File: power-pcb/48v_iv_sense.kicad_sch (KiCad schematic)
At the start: 20 parts, among them J21 Screw_Terminal_01x03, U2 ISO1540, U5 ADS1015IDGS, U7 INA240A1D

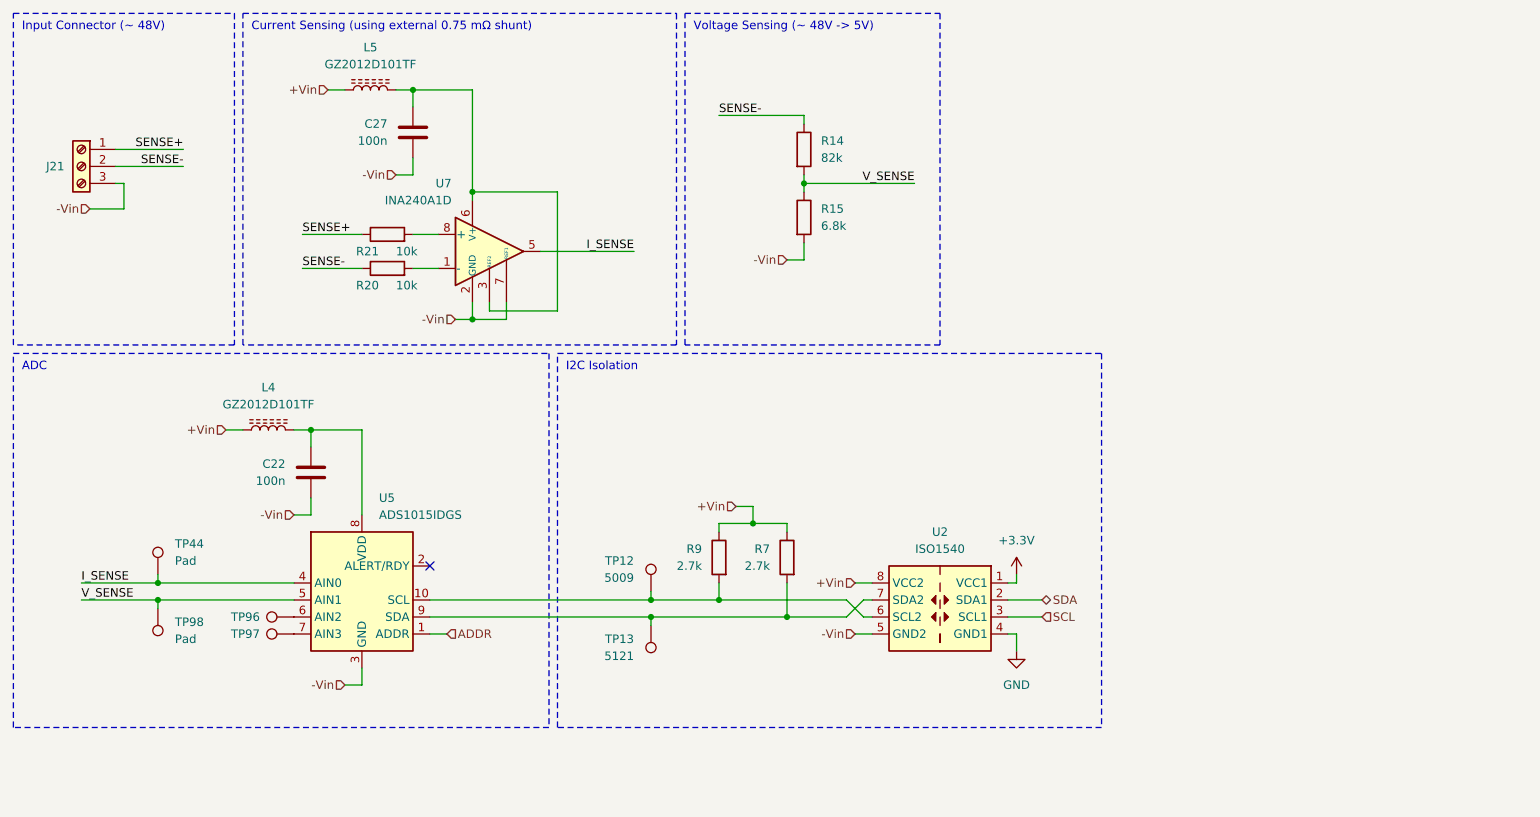
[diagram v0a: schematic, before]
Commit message: power-pcb: finish schematic layout
All parts are placed and connected, ERC passes (except for two
exclusions with comment).
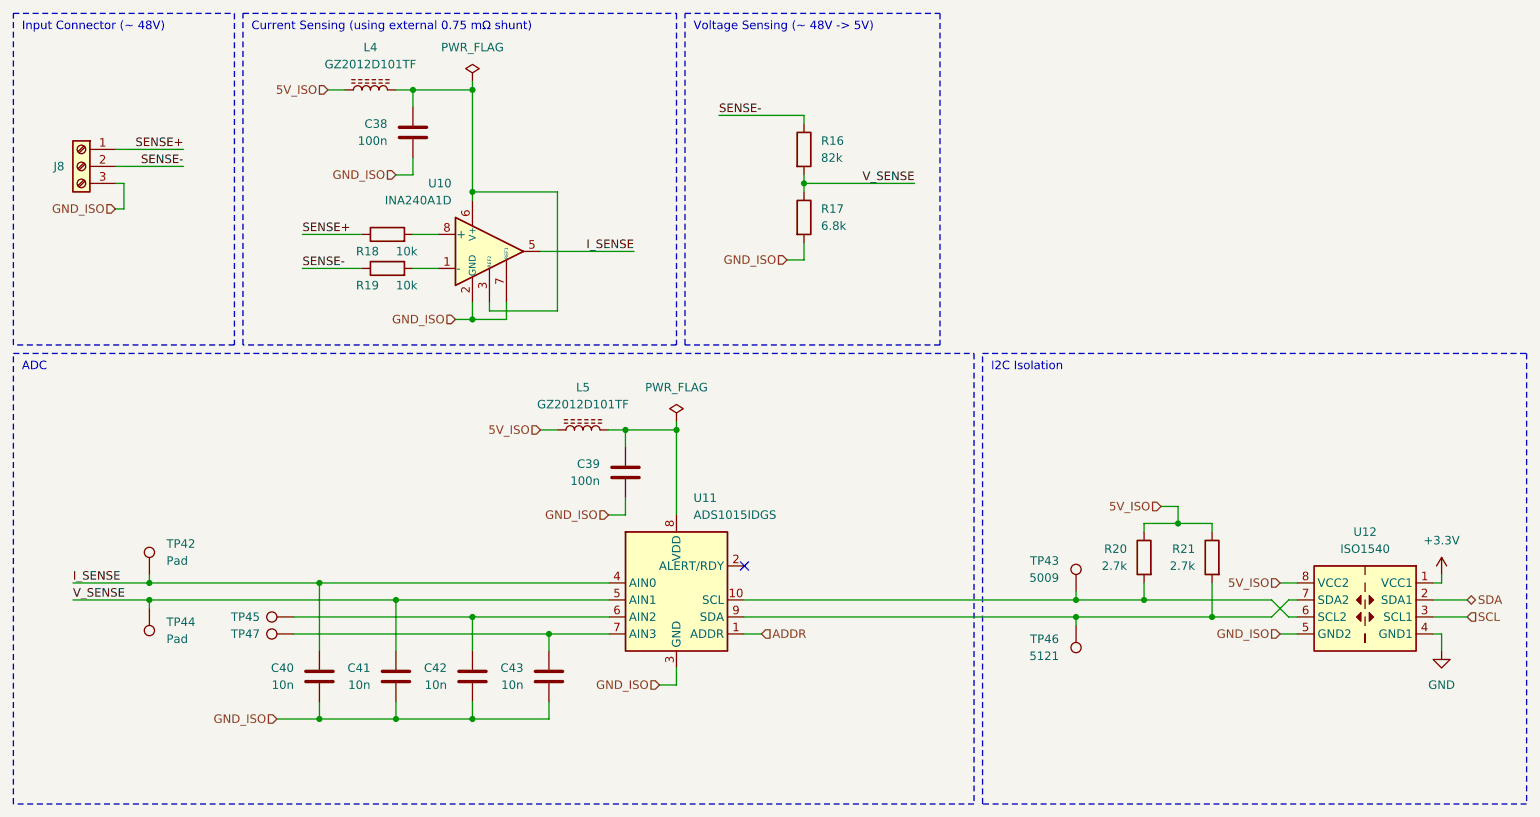
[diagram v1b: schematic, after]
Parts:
- added C40, C41, C42, C43: 10n, symbol Device:C
- renumbered C27 to C38, C22 to C39, J21 to J8, L5 to L4, L4 to L5, R14 to R16, R15 to R17, R21 to R18, R20 to R19, R9 to R20, R7 to R21, TP44 to TP42, TP12 to TP43, TP98 to TP44, TP96 to TP45, TP13 to TP46, TP97 to TP47, U7 to U10, U5 to U11, U2 to U12
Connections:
- net I_SENSE: now also C40.1
- net V_SENSE: now also C41.1
- net at TP45.1, U11.6 (AIN2): now also C42.1
- net at TP47.1, U11.7 (AIN3): now also C43.1
- net +Vin renamed 5V_ISO
- net -Vin renamed GND_ISO
- net GND_ISO: now also C40.2, C41.2, C42.2, C43.2
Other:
- moved on the sheet: C39, L5, R20, R21, TP42, TP43, TP44, TP46, U11, U12

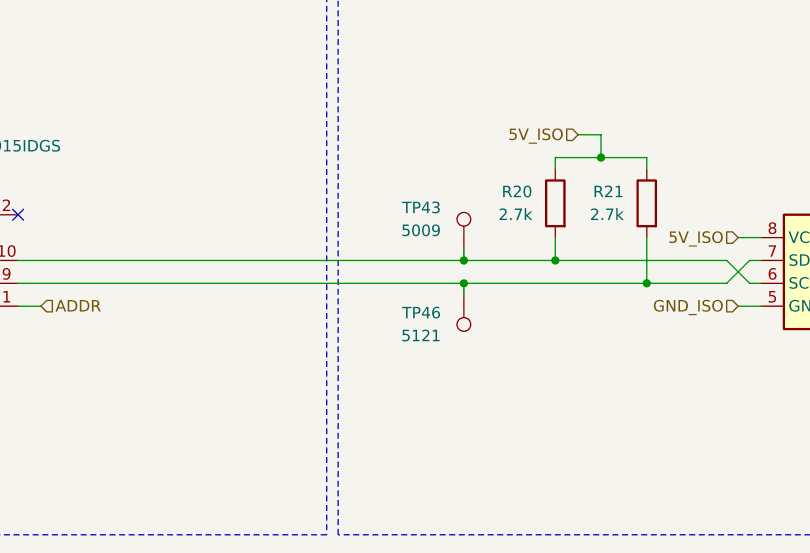
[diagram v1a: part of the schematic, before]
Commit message: power-pcb: finish assigning JLCPCB PN
Also assigned missing footprints.
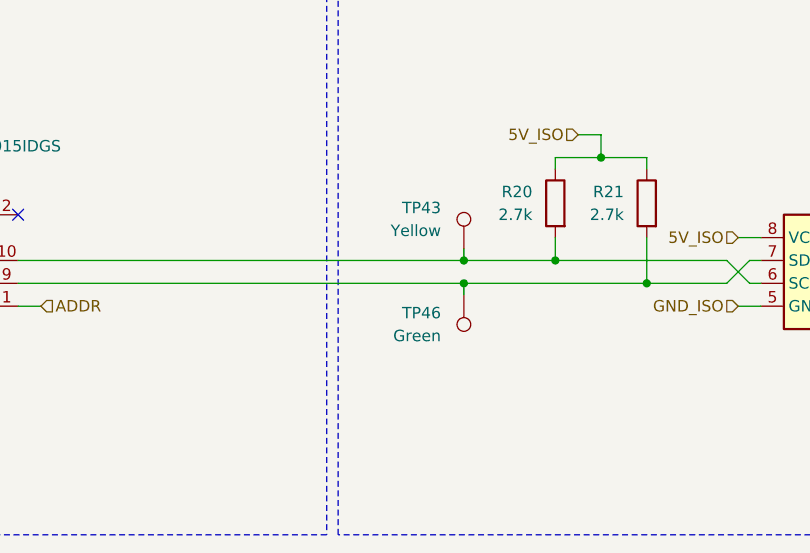
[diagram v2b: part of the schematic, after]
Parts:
- C40, C41, C42, C43: footprint (none) -> Capacitor_SMD:C_0402_1005Metric_Pad0.74x0.62mm_HandSolder; JLCPCB (none) -> C15195
- J8: footprint (none) -> Exocet:Wuerth_Term_Blk_3pos_Side_Entry_5mm; MFR (none) -> Wuerth Eletronik; MPN (none) -> 691137710003
- R16: footprint Capacitor_SMD:C_0603_1608Metric_Pad1.08x0.95mm_HandSolder -> Resistor_SMD:R_0603_1608Metric_Pad0.98x0.95mm_HandSolder
- R17: footprint Capacitor_SMD:C_0603_1608Metric_Pad1.08x0.95mm_HandSolder -> Resistor_SMD:R_0603_1608Metric_Pad0.98x0.95mm_HandSolder; JLCPCB C23254 -> C23212
- R18, R19: footprint (none) -> Resistor_SMD:R_0603_1608Metric_Pad0.98x0.95mm_HandSolder; JLCPCB (none) -> C25804
- R20, R21: footprint (none) -> Resistor_SMD:R_0603_1608Metric_Pad0.98x0.95mm_HandSolder; JLCPCB (none) -> C13167
- TP42, TP44: footprint (none) -> TestPoint:TestPoint_Pad_D1.5mm
- TP43: value 5009 -> Yellow; footprint (none) -> TestPoint:TestPoint_Keystone_5005-5009_Compact; MFR (none) -> Keystone Electronics; MPN (none) -> 5009
- TP45, TP47: value TestPoint -> Hole
- TP46: value 5121 -> Green; footprint (none) -> TestPoint:TestPoint_Keystone_5005-5009_Compact; MFR (none) -> Keystone Electronics; MPN (none) -> 5121
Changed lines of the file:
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@@
 			)
 		)
-		(property "Footprint" "Capacitor_SMD:C_0603_1608Metric_Pad1.08x0.95mm_HandSolder"
+		(property "Footprint" "Resistor_SMD:R_0603_1608Metric_Pad0.98x0.95mm_HandSolder"
 			(at 129.032 43.18 90)
 			(hide yes)
@@
 			)
 		)
-		(property "JLCPCB" "C23254"
+		(property "JLCPCB" "C23212"
 			(at 130.81 43.18 0)
 			(hide yes)
@@
 			)
 		)
-		(property "Footprint" ""
+		(property "Footprint" "Exocet:Wuerth_Term_Blk_3pos_Side_Entry_5mm"
 			(at 22.86 35.56 0)
 			(hide yes)
@@
 		)
 		(property "Description" "Generic screw terminal, single row, 01x03, script generated (kicad-library-utils/schlib/autogen/connector/)"
+			(at 22.86 35.56 0)
+			(hide yes)
+			(show_name no)
+			(do_not_autoplace no)
+			(effects
+				(font
+					(size 1.27 1.27)
+				)
+			)
+		)
+		(property "MFR" "Wuerth Eletronik"
+			(at 22.86 35.56 0)
+			(hide yes)
+			(show_name no)
+			(do_not_autoplace no)
+			(effects
+				(font
+					(size 1.27 1.27)
+				)
+			)
+		)
+		(property "MPN" "691137710003"
 			(at 22.86 35.56 0)
 			(hide yes)
@@
 			)
 		)
-		(property "Footprint" ""
+		(property "Footprint" "Capacitor_SMD:C_0402_1005Metric_Pad0.74x0.62mm_HandSolder"
 			(at 80.3148 115.57 0)
 			(hide yes)
@@
 			)
 		)
-		(property "Description" "Unpolarized capacitor"
+		(property "Description" "50V X7R ±10%"
+			(at 81.28 111.76 0)
+			(hide yes)
+			(show_name no)
+			(do_not_autoplace no)
+			(effects
+				(font
+					(size 1.27 1.27)
+				)
+			)
+		)
+		(property "JLCPCB" "C15195"
 			(at 81.28 111.76 0)
 			(hide yes)
@@
 			)
 		)
-		(property "Footprint" ""
+		(property "Footprint" "Capacitor_SMD:C_0402_1005Metric_Pad0.74x0.62mm_HandSolder"
 			(at 68.8848 115.57 0)
 			(hide yes)
@@
 			)
 		)
-		(property "Description" "Unpolarized capacitor"
+		(property "Description" "50V X7R ±10%"
+			(at 69.85 111.76 0)
+			(hide yes)
+			(show_name no)
+			(do_not_autoplace no)
+			(effects
+				(font
+					(size 1.27 1.27)
+				)
+			)
+		)
+		(property "JLCPCB" "C15195"
 			(at 69.85 111.76 0)
 			(hide yes)
@@
 			)
 		)
-		(property "Value" "5009"
+		(property "Value" "Yellow"
 			(at 168.91 97.0279 0)
 			(show_name no)
@@
 			)
 		)
-		(property "Footprint" ""
+		(property "Footprint" "TestPoint:TestPoint_Keystone_5005-5009_Compact"
 			(at 166.37 99.06 0)
 			(hide yes)
@@
 			)
 		)
-		(property "Description" "Auxiliary Battery GND"
+		(property "Description" "Test Point"
+			(at 171.45 99.06 0)
+			(hide yes)
+			(show_name no)
+			(do_not_autoplace no)
+			(effects
+				(font
+					(size 1.27 1.27)
+				)
+			)
+		)
+		(property "MPN" "5009"
+			(at 171.45 99.06 0)
+			(hide yes)
+			(show_name no)
+			(do_not_autoplace no)
+			(effects
+				(font
+					(size 1.27 1.27)
+				)
+			)
+		)
+		(property "MFR" "Keystone Electronics"
 			(at 171.45 99.06 0)
 			(hide yes)
@@
 			)
 		)
-		(property "Footprint" ""
+		(property "Footprint" "Resistor_SMD:R_0603_1608Metric_Pad0.98x0.95mm_HandSolder"
 			(at 193.548 93.98 90)
 			(hide yes)
@@
 		)
 		(property "Description" "Resistor"
+			(at 191.77 93.98 0)
+			(hide yes)
+			(show_name no)
+			(do_not_autoplace no)
+			(effects
+				(font
+					(size 1.27 1.27)
+				)
+			)
+		)
+		(property "JLCPCB" "C13167"
 			(at 191.77 93.98 0)
 			(hide yes)
@@
 			)
 		)
-		(property "Footprint" ""
+		(property "Footprint" "Resistor_SMD:R_0603_1608Metric_Pad0.98x0.95mm_HandSolder"
 			(at 68.58 52.578 90)
 			(hide yes)
@@
 		(property "Description" "Resistor"
 			(at 68.58 50.8 0)
+			(hide yes)
+			(show_name no)
+			(do_not_autoplace no)
+			(effects
+				(font
+					(size 1.27 1.27)
+				)
+			)
+		)
+		(property "JLCPCB" "C25804"
+			(at 68.58 50.8 90)
 			(hide yes)
 			(show_name no)
@@
 			)
 		)
-		(property "Footprint" ""
+		(property "Footprint" "TestPoint:TestPoint_Pad_D1.5mm"
 			(at 38.1 96.52 0)
 			(hide yes)
@@
 			)
 		)
-		(property "Description" "test point"
+		(property "Description" "Test Point"
 			(at 33.02 96.52 0)
 			(hide yes)
@@
 			)
 		)
-		(property "Value" "5121"
+		(property "Value" "Green"
 			(at 168.91 108.7119 0)
 			(show_name no)
@@
 			)
 		)
-		(property "Footprint" ""
+		(property "Footprint" "TestPoint:TestPoint_Keystone_5005-5009_Compact"
 			(at 176.53 104.14 0)
 			(hide yes)
@@
 			)
 		)
-		(property "Description" "Auxiliary Battery GND"
+		(property "Description" "Test Point"
+			(at 171.45 104.14 0)
+			(hide yes)
+			(show_name no)
+			(do_not_autoplace no)
+			(effects
+				(font
+					(size 1.27 1.27)
+				)
+			)
+		)
+		(property "MPN" "5121"
+			(at 171.45 104.14 0)
+			(hide yes)
+			(show_name no)
+			(do_not_autoplace no)
+			(effects
+				(font
+					(size 1.27 1.27)
+				)
+			)
+		)
+		(property "MFR" "Keystone Electronics"
 			(at 171.45 104.14 0)
 			(hide yes)
@@
 			)
 		)
-		(property "Value" "TestPoint"
+		(property "Value" "Hole"
 			(at 49.53 104.1399 90)
 			(hide yes)
@@
 			)
 		)
-		(property "Description" "test point"
+		(property "Description" "Test Point"
 			(at 54.61 102.87 0)
 			(hide yes)
@@
 			)
 		)
-		(property "Footprint" ""
+		(property "Footprint" "TestPoint:TestPoint_Pad_D1.5mm"
 			(at 27.94 101.6 0)
 			(hide yes)
@@
 			)
 		)
-		(property "Description" "test point"
+		(property "Description" "Test Point"
 			(at 33.02 101.6 0)
 			(hide yes)
@@
 			)
 		)
-		(property "Footprint" "Capacitor_SMD:C_0603_1608Metric_Pad1.08x0.95mm_HandSolder"
+		(property "Footprint" "Resistor_SMD:R_0603_1608Metric_Pad0.98x0.95mm_HandSolder"
 			(at 129.032 33.02 90)
 			(hide yes)
@@
 			)
 		)
-		(property "Footprint" ""
+		(property "Footprint" "Resistor_SMD:R_0603_1608Metric_Pad0.98x0.95mm_HandSolder"
 			(at 68.58 47.498 90)
 			(hide yes)
@@
 		(property "Description" "Resistor"
 			(at 68.58 45.72 0)
+			(hide yes)
+			(show_name no)
+			(do_not_autoplace no)
+			(effects
+				(font
+					(size 1.27 1.27)
+				)
+			)
+		)
+		(property "JLCPCB" "C25804"
+			(at 68.58 45.72 90)
 			(hide yes)
 			(show_name no)
@@
 			)
 		)
-		(property "Footprint" ""
+		(property "Footprint" "Resistor_SMD:R_0603_1608Metric_Pad0.98x0.95mm_HandSolder"
 			(at 183.388 93.98 90)
 			(hide yes)
@@
 		)
 		(property "Description" "Resistor"
+			(at 181.61 93.98 0)
+			(hide yes)
+			(show_name no)
+			(do_not_autoplace no)
+			(effects
+				(font
+					(size 1.27 1.27)
+				)
+			)
+		)
+		(property "JLCPCB" "C13167"
 			(at 181.61 93.98 0)
 			(hide yes)
@@
 			)
 		)
-		(property "Value" "TestPoint"
+		(property "Value" "Hole"
 			(at 49.53 106.6799 90)
 			(hide yes)
@@
 			)
 		)
-		(property "Description" "test point"
+		(property "Description" "Test Point"
 			(at 54.61 105.41 0)
 			(hide yes)
@@
 			)
 		)
-		(property "Footprint" ""
+		(property "Footprint" "Capacitor_SMD:C_0402_1005Metric_Pad0.74x0.62mm_HandSolder"
 			(at 57.4548 115.57 0)
 			(hide yes)
@@
 			)
 		)
-		(property "Description" "Unpolarized capacitor"
+		(property "Description" "50V X7R ±10%"
+			(at 58.42 111.76 0)
+			(hide yes)
+			(show_name no)
+			(do_not_autoplace no)
+			(effects
+				(font
+					(size 1.27 1.27)
+				)
+			)
+		)
+		(property "JLCPCB" "C15195"
 			(at 58.42 111.76 0)
 			(hide yes)
@@
 			)
 		)
-		(property "Footprint" ""
+		(property "Footprint" "Capacitor_SMD:C_0402_1005Metric_Pad0.74x0.62mm_HandSolder"
 			(at 91.7448 115.57 0)
 			(hide yes)
@@
 			)
 		)
-		(property "Description" "Unpolarized capacitor"
+		(property "Description" "50V X7R ±10%"
 			(at 92.71 111.76 0)
 			(hide yes)
+			(show_name no)
+			(do_not_autoplace no)
+			(effects
+				(font
+					(size 1.27 1.27)
+				)
+			)
+		)
+		(property "JLCPCB" "C15195"
+			(at 92.71 111.76 0)
+			(hide yes)
